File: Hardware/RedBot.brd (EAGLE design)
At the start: 94 x 49.5 mm, 66 parts, among them U1 ATMEGA328P, U2 TB6612FNG, U3 MIC5219 5V, U4 MIC5219 3.3V, U5 FT232RLSSOP, U6 7408SE, Y1 16MHz

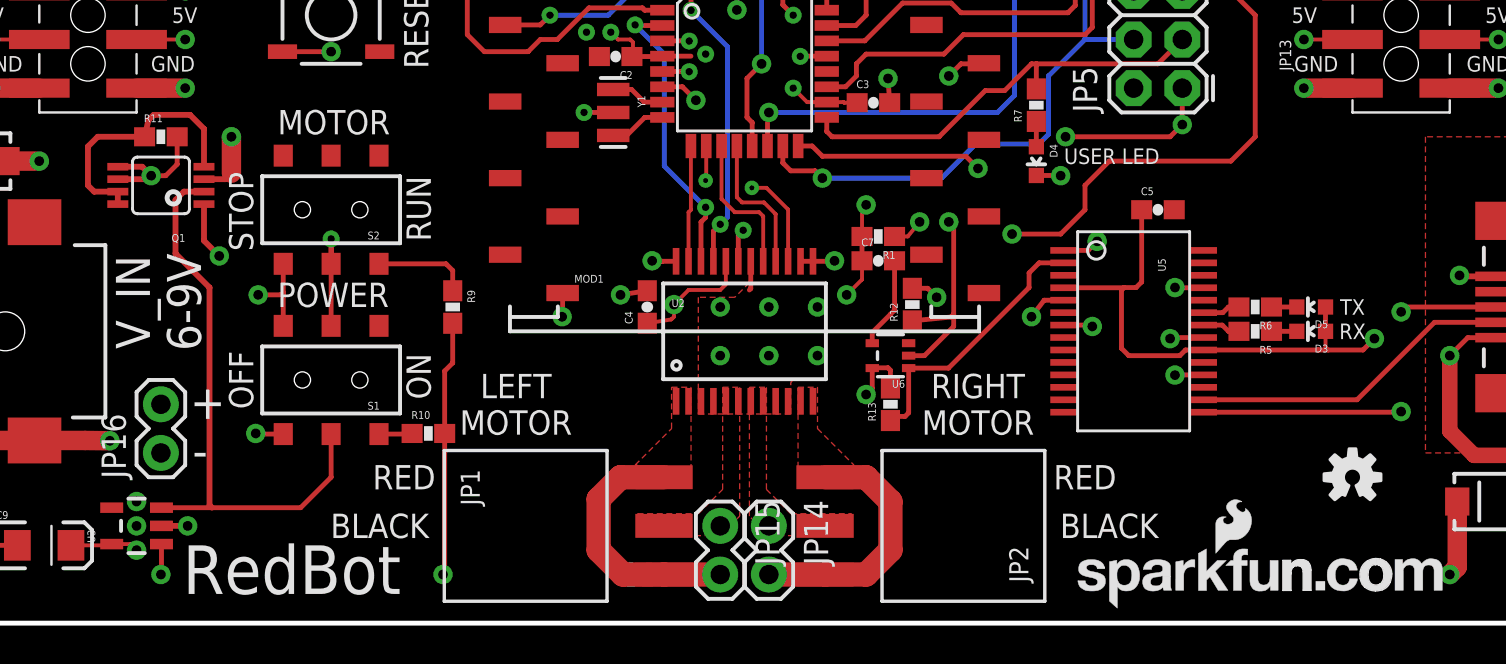
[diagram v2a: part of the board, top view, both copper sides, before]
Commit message: Hardware to v13 - Fix gating of battery voltage to servos - Add a user input button to pin 12 - label user led as D13 LED for clarity
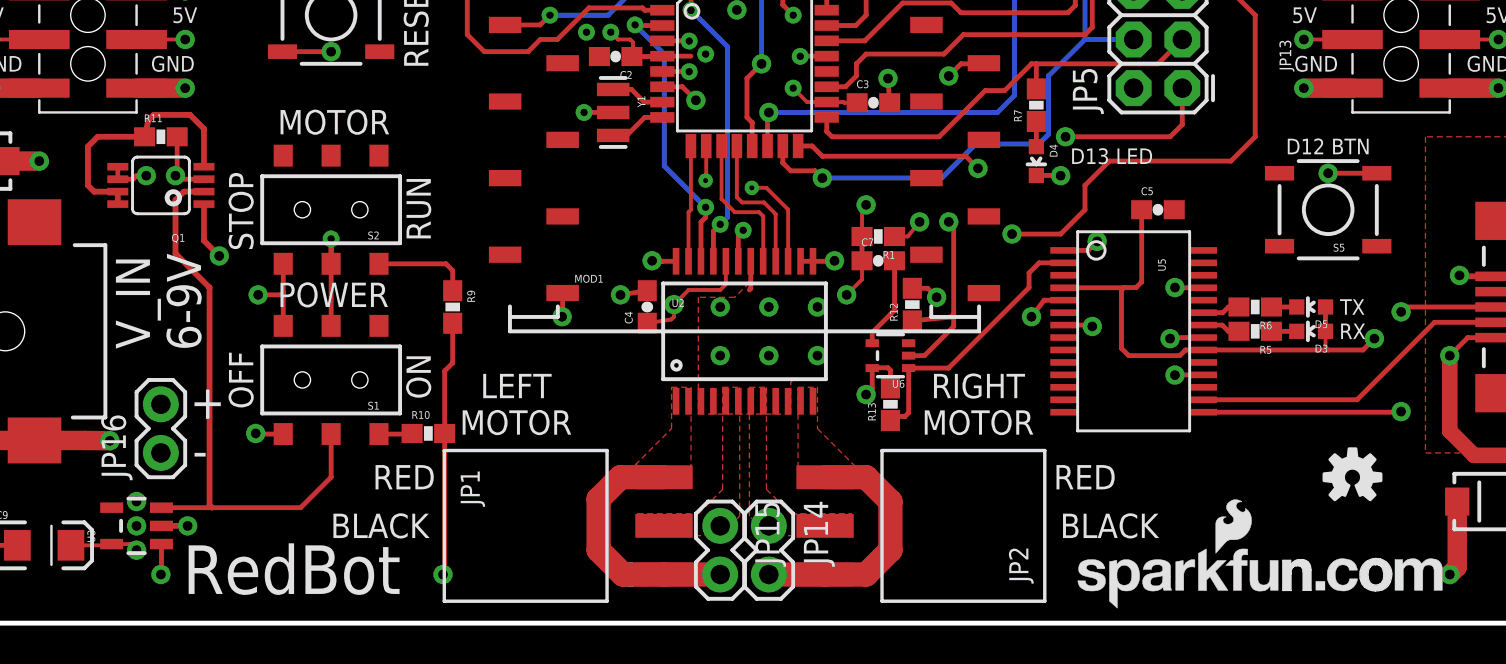
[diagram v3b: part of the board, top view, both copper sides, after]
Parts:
- added S5: (no value), SparkFun-Electromechanical:TACTILE_SWITCH_SMD
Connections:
- net GND: now also S5.1
- net MISO: now also S5.3
- net V_BATT: now also Q1.3; no longer Q1.5, Q1.6
- net V_GATED: now also Q1.5, Q1.6; no longer Q1.3
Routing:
- net MISO: track 23.4 -> 35.4 mm
- net V_BATT: track 81.3 -> 77.2 mm
- net V_GATED: track 113.8 -> 117.2 mm
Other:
- board text added: "D12 BTN"
- board text added: "D13 LED"
- board text added: "v13"
- board text removed: "USER LED"
- board text removed: "v12"
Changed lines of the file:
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@@
 <layers>
 <layer number="1" name="Top" color="4" fill="1" visible="yes" active="yes"/>
-<layer number="2" name="5V" color="1" fill="3" visible="no" active="yes"/>
-<layer number="15" name="Gnd" color="4" fill="6" visible="no" active="yes"/>
+<layer number="2" name="5V" color="1" fill="3" visible="yes" active="yes"/>
+<layer number="15" name="Gnd" color="4" fill="6" visible="yes" active="yes"/>
 <layer number="16" name="Bottom" color="1" fill="1" visible="yes" active="yes"/>
 <layer number="17" name="Pads" color="2" fill="1" visible="yes" active="yes"/>
@@
 <text x="66.04" y="5.08" size="1.27" layer="21" font="vector" ratio="15" align="center">BLACK</text>
 <text x="58.42" y="44.323" size="1.27" layer="21" font="vector" ratio="15" align="center">POWER</text>
-<text x="66.167" y="24.384" size="0.8128" layer="21" font="vector" ratio="15" align="center">USER LED</text>
-<text x="41.91" y="2.54" size="1.27" layer="16" font="vector" ratio="15" rot="MR0" align="center">v12</text>
+<text x="66.167" y="24.384" size="0.8128" layer="21" font="vector" ratio="15" align="center">D13 LED</text>
+<text x="41.91" y="2.54" size="1.27" layer="16" font="vector" ratio="15" rot="MR0" align="center">v13</text>
 <text x="3.175" y="41.021" size="0.8128" layer="21" font="vector" ratio="15">5V</text>
 <text x="6.985" y="39.37" size="0.8128" layer="21" font="vector" ratio="15" align="center-left">GND</text>
@@
 <wire x1="90.932" y1="27.94" x2="91.44" y2="28.448" width="0.254" layer="21"/>
 <text x="46.99" y="7.62" size="2.54" layer="22" font="vector" ratio="15" rot="MR0" align="bottom-center">sparkfun.com/redbot</text>
+<text x="77.47" y="24.892" size="0.8128" layer="21" font="vector" ratio="15" align="center">D12 BTN</text>
 </plain>
 <attributes>
@@
 <element name="FID1" library="SparkFun-Aesthetics" package="MICRO-FIDUCIAL" value="FIDUCIALUFIDUCIAL" x="6.35" y="48.26"/>
 <element name="FID2" library="SparkFun-Aesthetics" package="MICRO-FIDUCIAL" value="FIDUCIALUFIDUCIAL" x="87.63" y="1.27"/>
+<element name="S5" library="SparkFun-Electromechanical" package="TACTILE_SWITCH_SMD" value="" x="77.47" y="21.59" rot="R180">
+<attribute name="PROD_ID" value="SWCH-08247" x="77.47" y="21.59" size="1.778" layer="27" font="vector" ratio="15" rot="R180" display="off"/>
+</element>
 </elements>
 <signals>
@@
 <contactref element="U5" pad="26"/>
 <contactref element="U6" pad="3"/>
+<contactref element="S5" pad="1"/>
 </signal>
 <signal name="SENSOR_0/SW_TXO">
@@
 <wire x1="63.754" y1="25.4" x2="69.215" y2="25.4" width="0.254" layer="1"/>
 <wire x1="69.215" y1="25.4" x2="69.85" y2="26.035" width="0.254" layer="1"/>
-<via x="69.85" y="26.035" extent="1-16" drill="0.508"/>
 <wire x1="69.85" y1="26.035" x2="69.85" y2="27.94" width="0.254" layer="1"/>
+<contactref element="S5" pad="3"/>
+<wire x1="69.85" y1="27.94" x2="70.358" y2="27.94" width="0.254" layer="2"/>
+<wire x1="70.358" y1="27.94" x2="74.803" y2="23.495" width="0.254" layer="2"/>
+<wire x1="74.803" y1="23.495" x2="77.47" y2="23.495" width="0.254" layer="2"/>
+<via x="77.47" y="23.495" extent="1-16" drill="0.508"/>
+<wire x1="77.47" y1="23.495" x2="80.01" y2="23.495" width="0.254" layer="1"/>
 </signal>
 <signal name="SCK">
@@
 <wire x1="6.223" y1="20.447" x2="7.62" y2="19.05" width="1.016" layer="15"/>
 <wire x1="7.62" y1="19.05" x2="16.51" y2="19.05" width="1.016" layer="15"/>
-<wire x1="16.51" y1="19.05" x2="21.59" y2="24.13" width="1.016" layer="15"/>
+<wire x1="17.272" y1="19.812" x2="21.59" y2="24.13" width="1.016" layer="15"/>
 <wire x1="21.59" y1="24.13" x2="29.337" y2="24.13" width="1.016" layer="15"/>
 <wire x1="29.337" y1="24.13" x2="34.544" y2="18.923" width="1.016" layer="15"/>
@@
 <contactref element="JP3" pad="VIN0"/>
 <contactref element="R11" pad="2"/>
-<contactref element="Q1" pad="5"/>
-<contactref element="Q1" pad="6"/>
 <wire x1="4.2" y1="23.25" x2="3.81" y2="22.86" width="1.016" layer="1"/>
 <wire x1="3.81" y1="22.86" x2="3.81" y2="20.94" width="1.016" layer="1"/>
@@
 <via x="6.223" y="24.13" extent="1-16" drill="0.508"/>
 <wire x1="4.2" y1="24.13" x2="6.223" y2="24.13" width="1.27" layer="1"/>
-<wire x1="16.51" y1="19.05" x2="16.51" y2="22.86" width="1.27" layer="15"/>
-<wire x1="16.51" y1="22.86" x2="16.002" y2="23.368" width="1.27" layer="15"/>
-<via x="16.002" y="23.368" extent="1-16" drill="0.508"/>
-<wire x1="14.26" y1="23.835" x2="15.535" y2="23.835" width="0.3048" layer="1"/>
-<wire x1="15.535" y1="23.835" x2="16.002" y2="23.368" width="0.3048" layer="1"/>
-<wire x1="14.26" y1="23.185" x2="15.819" y2="23.185" width="0.3048" layer="1"/>
-<wire x1="15.819" y1="23.185" x2="16.002" y2="23.368" width="0.3048" layer="1"/>
+<wire x1="16.51" y1="19.05" x2="17.272" y2="19.812" width="1.27" layer="15"/>
+<wire x1="17.272" y1="19.812" x2="17.272" y2="23.368" width="1.27" layer="15"/>
+<via x="17.272" y="23.368" extent="1-16" drill="0.508"/>
 <wire x1="4.2" y1="24.13" x2="4.2" y2="23.25" width="0.3048" layer="1"/>
 <contactref element="JP16" pad="2"/>
 <wire x1="16.51" y1="11.43" x2="16.51" y2="19.05" width="1.016" layer="15"/>
-<wire x1="17.36" y1="25.4" x2="17.36" y2="23.964" width="0.254" layer="1"/>
-<wire x1="17.36" y1="23.964" x2="16.764" y2="23.368" width="0.254" layer="1"/>
-<wire x1="16.764" y1="23.368" x2="16.002" y2="23.368" width="0.254" layer="1"/>
+<contactref element="Q1" pad="3"/>
+<wire x1="17.36" y1="25.4" x2="17.36" y2="23.456" width="0.254" layer="1"/>
+<wire x1="17.36" y1="23.456" x2="17.272" y2="23.368" width="0.254" layer="1"/>
+<wire x1="18.76" y1="23.185" x2="17.455" y2="23.185" width="0.254" layer="1"/>
+<wire x1="17.455" y1="23.185" x2="17.272" y2="23.368" width="0.254" layer="1"/>
 </signal>
 <signal name="N$23">
@@
 </signal>
 <signal name="V_GATED">
-<contactref element="Q1" pad="3"/>
 <contactref element="JP8" pad="3"/>
 <contactref element="JP9" pad="3"/>
 <contactref element="JP8" pad="4"/>
 <contactref element="JP9" pad="4"/>
-<wire x1="18.76" y1="23.185" x2="19.883" y2="23.185" width="0.3048" layer="1"/>
-<wire x1="19.883" y1="23.185" x2="20.193" y2="23.495" width="0.3048" layer="1"/>
-<wire x1="20.193" y1="23.495" x2="20.193" y2="25.4" width="1.016" layer="1"/>
-<via x="20.193" y="25.4" extent="1-16" drill="0.508"/>
-<wire x1="20.193" y1="25.4" x2="20.193" y2="31.75" width="1.016" layer="15"/>
-<wire x1="20.193" y1="31.75" x2="19.685" y2="32.258" width="1.016" layer="15"/>
-<wire x1="19.685" y1="32.258" x2="19.685" y2="36.068" width="1.016" layer="15"/>
+<via x="15.748" y="23.368" extent="1-16" drill="0.508"/>
+<wire x1="15.748" y1="23.368" x2="15.748" y2="24.638" width="1.016" layer="15"/>
+<wire x1="15.748" y1="24.638" x2="16.51" y2="25.4" width="1.016" layer="15"/>
+<wire x1="16.51" y1="25.4" x2="18.669" y2="25.4" width="1.016" layer="15"/>
+<wire x1="18.669" y1="25.4" x2="19.685" y2="26.416" width="1.016" layer="15"/>
+<wire x1="19.685" y1="26.416" x2="19.685" y2="36.068" width="1.016" layer="15"/>
 <wire x1="19.685" y1="36.068" x2="19.05" y2="36.703" width="1.016" layer="15"/>
 <wire x1="19.05" y1="36.703" x2="19.05" y2="39.37" width="1.016" layer="15"/>
@@
 <via x="30.48" y="40.64" extent="1-16" drill="0.508"/>
 <wire x1="30.48" y1="40.64" x2="30.48" y2="47.879" width="1.016" layer="2"/>
+<contactref element="Q1" pad="5"/>
+<contactref element="Q1" pad="6"/>
+<wire x1="15.748" y1="23.368" x2="15.24" y2="23.368" width="0.254" layer="1"/>
+<wire x1="15.24" y1="23.368" x2="15.057" y2="23.185" width="0.254" layer="1"/>
+<wire x1="14.26" y1="23.185" x2="15.057" y2="23.185" width="0.254" layer="1"/>
+<wire x1="14.26" y1="23.185" x2="14.26" y2="23.835" width="0.254" layer="1"/>
 </signal>
 <signal name="N$3">

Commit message: Added support for encoder and whisker bumper; changing schematic and layout to fix some issues and pretty it up a bit. Hardware changes not done!
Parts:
- added JP17: FTDI_DEVICE, SparkFun-Connectors:FTDI_DEVICE_SIDE
- moved FRAME1 241.3 mm to (214.6, -19.1)
- moved C5 236.3 mm to (304.8, 15.2)
- moved C6 236.3 mm to (272.3, 31.4)
- moved C8 236.3 mm to (273.1, 33.8)
- moved FID2 236.3 mm to (323.9, -5.08)
- moved JP14 236.3 mm to (284.5, -1.27)
- moved JP6 236.3 mm to (327.7, 27.9)
- moved JP9 236.3 mm to (304.8, 34.3)
- moved R12 236.3 mm to (292.0, 10.3)
- moved R3 236.3 mm to (288.3, 40.6)
- moved R8 236.3 mm to (295.9, 39.4)
- moved R9 236.3 mm to (268.0, 10.2)
- moved STANDOFF1 236.3 mm to (327.7, -3.81)
- moved STANDOFF4 236.3 mm to (327.7, 40.6)
- moved U4 236.3 mm to (273.1, 36.8)
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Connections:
- net 5V: now also JP17.P$4
- net GND: now also JP17.P$6
- net XBEE_RXI: now also JP17.P$3
- net XBEE_TXO: now also JP17.P$2

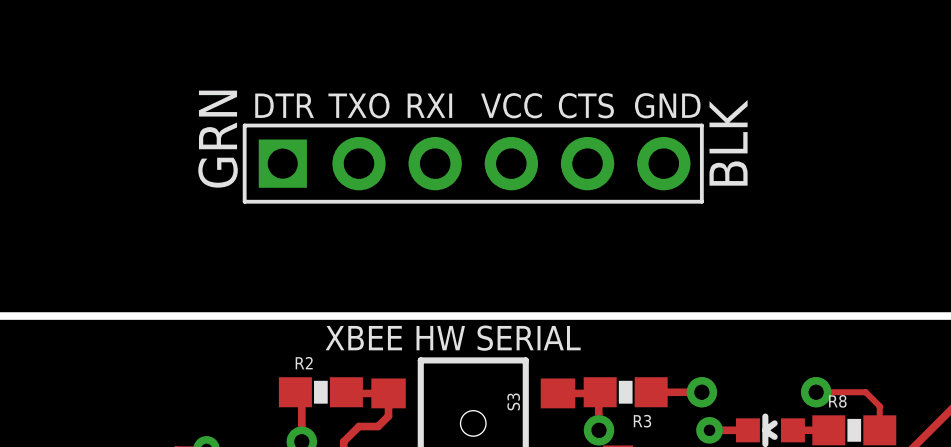
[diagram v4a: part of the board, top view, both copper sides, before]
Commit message: Changes to library, changes to board. Will need to do some branching magic to separate the two. This will become the sw dev branch.
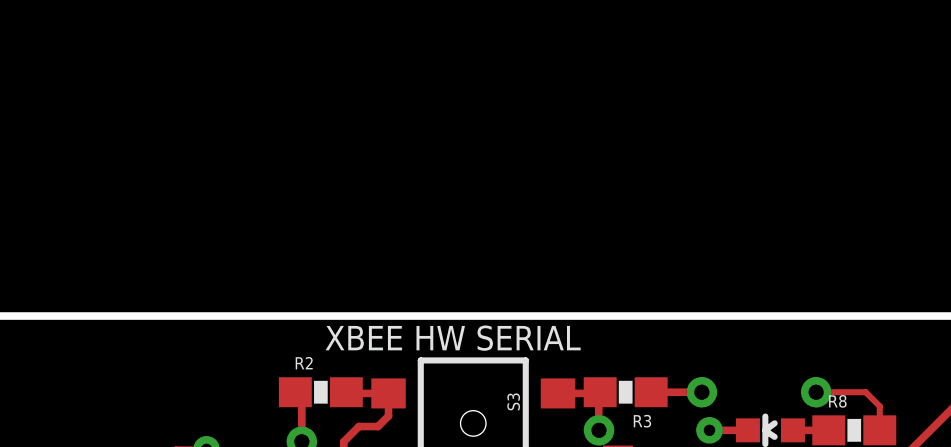
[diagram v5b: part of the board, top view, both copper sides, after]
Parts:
- removed JP17: FTDI_DEVICE, SparkFun-Connectors:FTDI_DEVICE_SIDE
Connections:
- net 5V: no longer JP17.P$4
- net GND: no longer JP17.P$6
- net XBEE_RXI: no longer JP17.P$3
- net XBEE_TXO: no longer JP17.P$2

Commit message: Rollback design to current master
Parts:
- removed S5: (no value), SparkFun-Electromechanical:TACTILE_SWITCH_SMD
- moved FRAME1 241.3 mm to (-26.7, -16.5)
- moved C5 236.3 mm to (68.6, 21.6)
- moved C6 236.3 mm to (36.1, 37.7)
- moved C8 236.3 mm to (36.8, 40.1)
- moved FID2 236.3 mm to (87.6, 1.27)
- moved JP14 236.3 mm to (48.3, 5.08)
- moved JP6 236.3 mm to (91.4, 34.3)
- moved JP9 236.3 mm to (68.6, 40.6)
- moved R12 236.3 mm to (55.8, 16.6)
- moved R3 236.3 mm to (52.1, 47.0)
- moved R8 236.3 mm to (59.7, 45.7)
- moved R9 236.3 mm to (31.8, 16.5)
- moved STANDOFF1 236.3 mm to (91.4, 2.54)
- moved STANDOFF4 236.3 mm to (91.4, 47.0)
- moved U4 236.3 mm to (36.8, 43.2)
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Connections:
- net GND: no longer S5.1
- net MISO: no longer S5.3
- net V_BATT: now also Q1.5, Q1.6; no longer Q1.3
- net V_GATED: now also Q1.3; no longer Q1.5, Q1.6
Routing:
- net MISO: track 35.4 -> 23.4 mm
- net V_BATT: track 77.2 -> 81.3 mm
- net V_GATED: track 117.2 -> 113.8 mm
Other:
- board text added: "USER LED"
- board text added: "v12"
- board text removed: "D12 BTN"
- board text removed: "D13 LED"
- board text removed: "v13"

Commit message: Update boards to v13. - Flip MOSFET to gate power to Servo headers - Add button to pin 12 - change silk on LED to D13 LED - add some silk to the back
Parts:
- added S5: (no value), SparkFun-Electromechanical:TACTILE_SWITCH_SMD
- moved FRAME1 241.3 mm to (214.6, -19.1)
- moved C5 236.3 mm to (304.8, 15.2)
- moved C6 236.3 mm to (272.3, 31.4)
- moved C8 236.3 mm to (273.1, 33.8)
- moved FID2 236.3 mm to (323.9, -5.08)
- moved JP14 236.3 mm to (284.5, -1.27)
- moved JP6 236.3 mm to (327.7, 27.9)
- moved JP9 236.3 mm to (304.8, 34.3)
- moved R12 236.3 mm to (292.0, 10.3)
- moved R3 236.3 mm to (288.3, 40.6)
- moved R8 236.3 mm to (295.9, 39.4)
- moved R9 236.3 mm to (268.0, 10.2)
- moved STANDOFF1 236.3 mm to (327.7, -3.81)
- moved STANDOFF4 236.3 mm to (327.7, 40.6)
- moved U4 236.3 mm to (273.1, 36.8)
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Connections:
- net GND: now also S5.1
- net MISO: now also S5.3
- net V_BATT: now also Q1.3; no longer Q1.5, Q1.6
- net V_GATED: now also Q1.5, Q1.6; no longer Q1.3
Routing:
- net MISO: track 23.4 -> 35.4 mm
- net V_BATT: track 81.3 -> 77.2 mm
- net V_GATED: track 113.8 -> 117.2 mm
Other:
- board text added: "D12 BTN"
- board text added: "D13 LED"
- board text added: "v13"
- board text removed: "USER LED"
- board text removed: "v12"

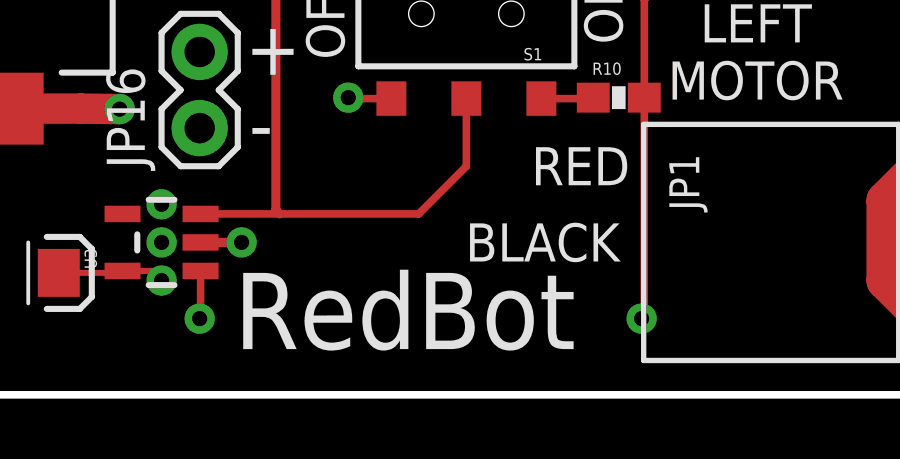
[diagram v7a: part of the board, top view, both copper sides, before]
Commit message: Added RedBot logo
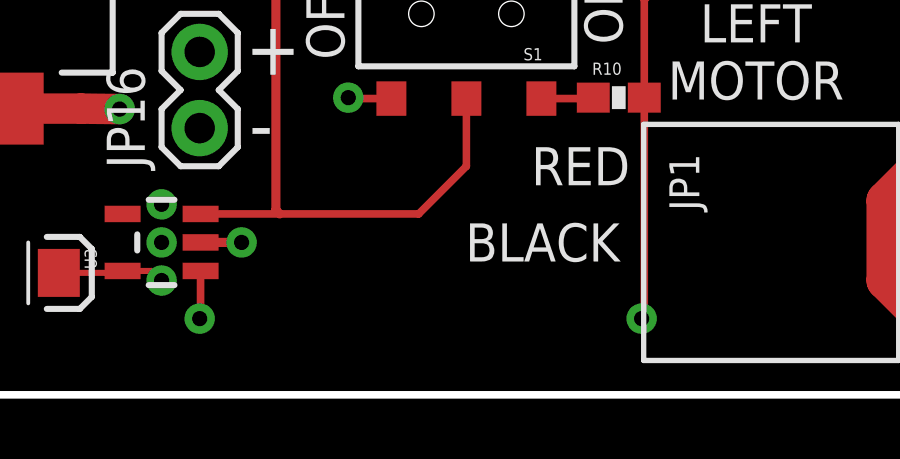
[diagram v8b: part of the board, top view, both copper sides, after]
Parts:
- added U$23: REDBOT_LOGO, SparkFun-Aesthetics:REDBOT_LOGO
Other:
- board text removed: "RedBot"
